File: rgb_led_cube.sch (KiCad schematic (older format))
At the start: 90 parts, among them Q1 IRLML6401TRPBF, Q10 MMBT2222A-TP, Q11 IRLML6401TRPBF, Q12 MMBT2222A-TP, Q13 IRLML6401TRPBF, Q14 MMBT2222A-TP, Q15 IRLML6401TRPBF, Q16 MMBT2222A-TP, Q2 MMBT2222A-TP, Q3 IRLML6401TRPBF, Q4 MMBT2222A-TP, Q5 IRLML6401TRPBF, Q6 MMBT2222A-TP, Q7 IRLML6401TRPBF, Q8 MMBT2222A-TP, Q9 IRLML6401TRPBF, U1 TLC59711PWPR, U10 TLC59711PWPR, U11 TLC59711PWPR, U12 TLC59711PWPR, U13 TLC59711PWPR, U14 TLC59711PWPR, U15 TLC59711PWPR, U16 TLC59711PWPR, U2 TLC59711PWPR, U3 TLC59711PWPR, U4 TLC59711PWPR, U5 TLC59711PWPR, U6 TLC59711PWPR, U7 TLC59711PWPR, U8 TLC59711PWPR, U9 TLC59711PWPR

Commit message: Update components placement
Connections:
- net at R20.2: now also CNTL1.13 (G12)
- net at R17.2: now also CNTL1.15 (G13)
- net at R23.2: now also CNTL1.12 (G14)
- net at R26.2: now also CNTL1.11 (G27)
- net at R29.2: now also CNTL1.10 (G26)
- net at R32.2: now also CNTL1.9 (G25)
- net at R35.2: now also CNTL1.8 (G33)
- net at R38.2: now also CNTL1.7 (G32)
- no-connect marks 2 -> 23
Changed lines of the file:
@@
 Wire Wire Line
 	11400 8450 10950 8450
+Wire Wire Line
+	9450 9750 8950 9750
+Wire Wire Line
+	8950 9750 8950 1350
+Wire Wire Line
+	8950 1350 9950 1350
+Wire Wire Line
+	9450 9550 9000 9550
+Wire Wire Line
+	9000 9550 9000 2150
+Wire Wire Line
+	9000 2150 9950 2150
+Wire Wire Line
+	9950 2950 9050 2950
+Wire Wire Line
+	9050 2950 9050 9450
+Wire Wire Line
+	9050 9450 9450 9450
+Wire Wire Line
+	9450 9350 9100 9350
+Wire Wire Line
+	9100 9350 9100 3750
+Wire Wire Line
+	9100 3750 9950 3750
+Wire Wire Line
+	9450 9250 9150 9250
+Wire Wire Line
+	9150 9250 9150 4550
+Wire Wire Line
+	9150 4550 9950 4550
+Wire Wire Line
+	9450 9150 9200 9150
+Wire Wire Line
+	9200 9150 9200 5350
+Wire Wire Line
+	9200 5350 9950 5350
+Wire Wire Line
+	9450 9050 9250 9050
+Wire Wire Line
+	9250 9050 9250 6150
+Wire Wire Line
+	9250 6150 9950 6150
+Wire Wire Line
+	9450 8950 9300 8950
+Wire Wire Line
+	9300 8950 9300 6950
+Wire Wire Line
+	9300 6950 9950 6950
+NoConn ~ 10950 10150
+NoConn ~ 10950 10050
+NoConn ~ 10950 9950
+NoConn ~ 10950 9850
+NoConn ~ 10950 9750
+NoConn ~ 10950 9650
+NoConn ~ 10950 9550
+NoConn ~ 10950 9450
+NoConn ~ 10950 9350
+NoConn ~ 10950 9250
+NoConn ~ 10950 9050
+NoConn ~ 10950 8850
+NoConn ~ 10950 8750
+NoConn ~ 10950 8650
+NoConn ~ 10950 8550
+NoConn ~ 9450 9850
+NoConn ~ 9450 9950
+NoConn ~ 9450 8350
+NoConn ~ 9450 8450
+NoConn ~ 9450 8550
+NoConn ~ 9450 8650
 $EndSCHEMATC

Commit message: Route ICs
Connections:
- net GND: no longer CNTL1.18 (CMD)
- no-connect marks 23 -> 24
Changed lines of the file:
@@
-$EndComp
-$Comp
-L power:GND #PWR0132
-U 1 1 5EAE4677
-P 9450 10050
-F 0 "#PWR0132" H 9450 9800 50  0001 C CNN
-F 1 "GND" V 9455 9922 50  0000 R CNN
-F 2 "" H 9450 10050 50  0001 C CNN
-F 3 "" H 9450 10050 50  0001 C CNN
-	1    9450 10050
-	0    1    1    0
 $EndComp
 $Comp
@@
 NoConn ~ 9450 8550
 NoConn ~ 9450 8650
+NoConn ~ 9450 10050
 $EndSCHEMATC

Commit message: Route pcb
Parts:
- Q1, Q10, Q11, Q12, Q13, Q14, Q15, Q16, Q2, Q3, Q4, Q5, Q6, Q7, Q8, Q9: footprint digikey-footprints:SOT-23-3 -> Package_TO_SOT_SMD:SOT-23
- U1, U10, U11, U12, U13, U14, U15, U16, U2, U3, U4, U5, U6, U7, U8, U9: footprint digikey-footprints:TSSOP-20-1EP_W4.4mm -> Package_SO:HTSSOP-20-1EP_4.4x6.5mm_P0.65mm_EP3.4x6.5mm_Mask2.75x3.43mm_ThermalVias

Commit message: Connect unused header pins to GND
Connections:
- net GND: now also CNTL1.39, CNTL1.40
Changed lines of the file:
@@
 NoConn ~ 9450 8650
 NoConn ~ 9450 10050
+$Comp
+L power:GND #PWR?
+U 1 1 5EAE9B47
+P 9950 10450
+F 0 "#PWR?" H 9950 10200 50  0001 C CNN
+F 1 "GND" H 9955 10277 50  0000 C CNN
+F 2 "" H 9950 10450 50  0001 C CNN
+F 3 "" H 9950 10450 50  0001 C CNN
+	1    9950 10450
+	1    0    0    -1
+$EndComp
+$Comp
+L power:GND #PWR?
+U 1 1 5EAEB6F4
+P 10050 10450
+F 0 "#PWR?" H 10050 10200 50  0001 C CNN
+F 1 "GND" H 10055 10277 50  0000 C CNN
+F 2 "" H 10050 10450 50  0001 C CNN
+F 3 "" H 10050 10450 50  0001 C CNN
+	1    10050 10450
+	1    0    0    -1
+$EndComp
 $EndSCHEMATC

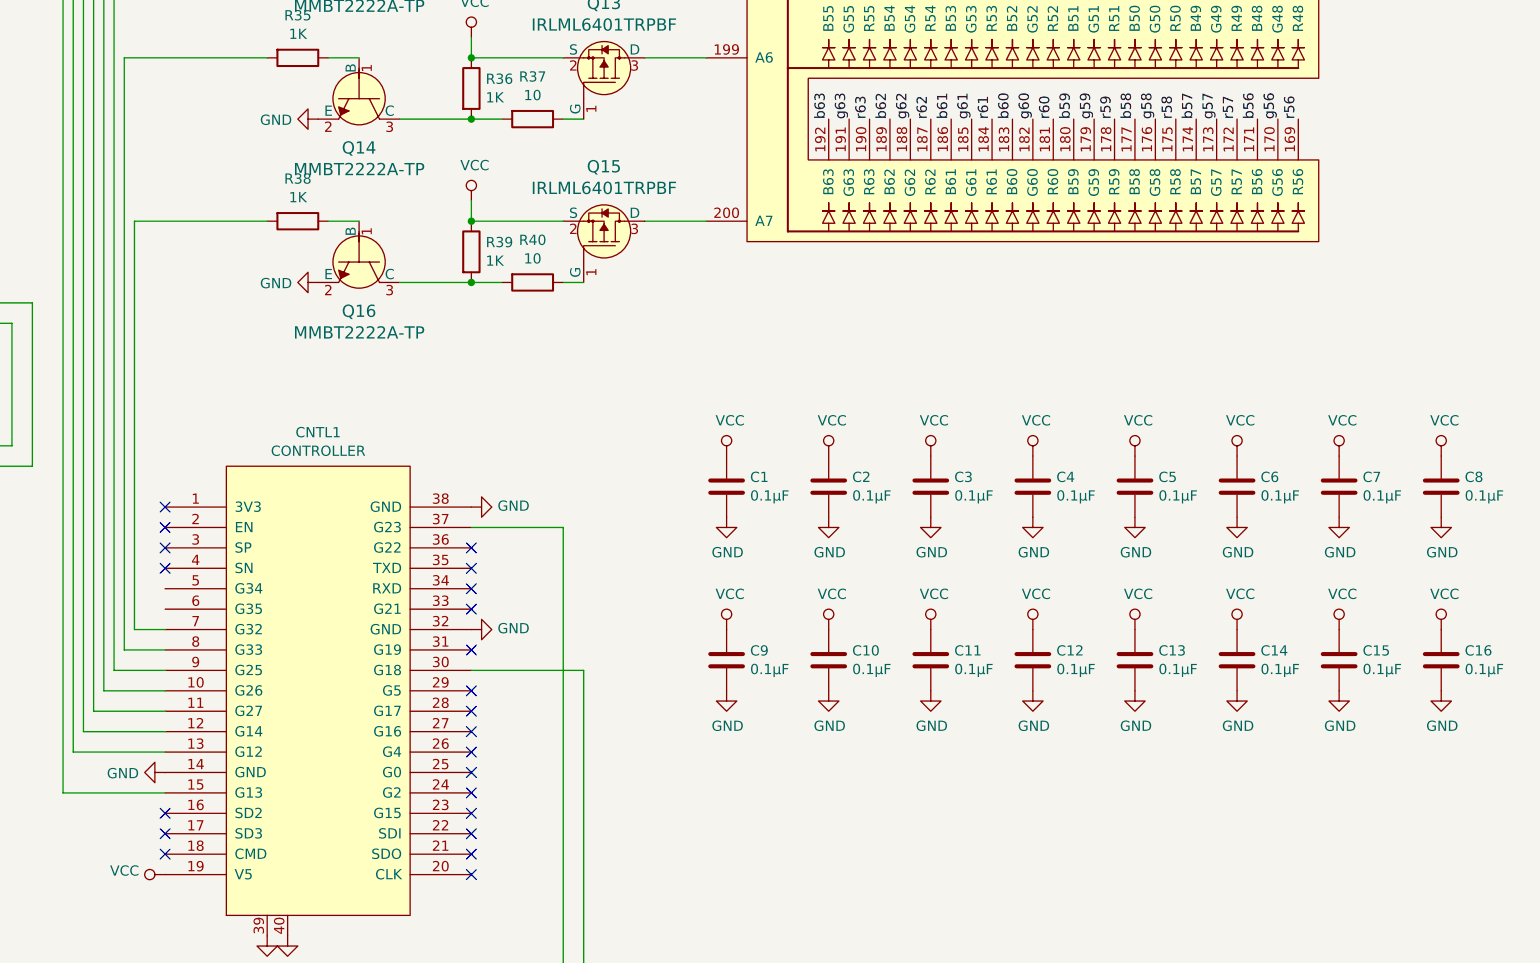
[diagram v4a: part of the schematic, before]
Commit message: Add microphone
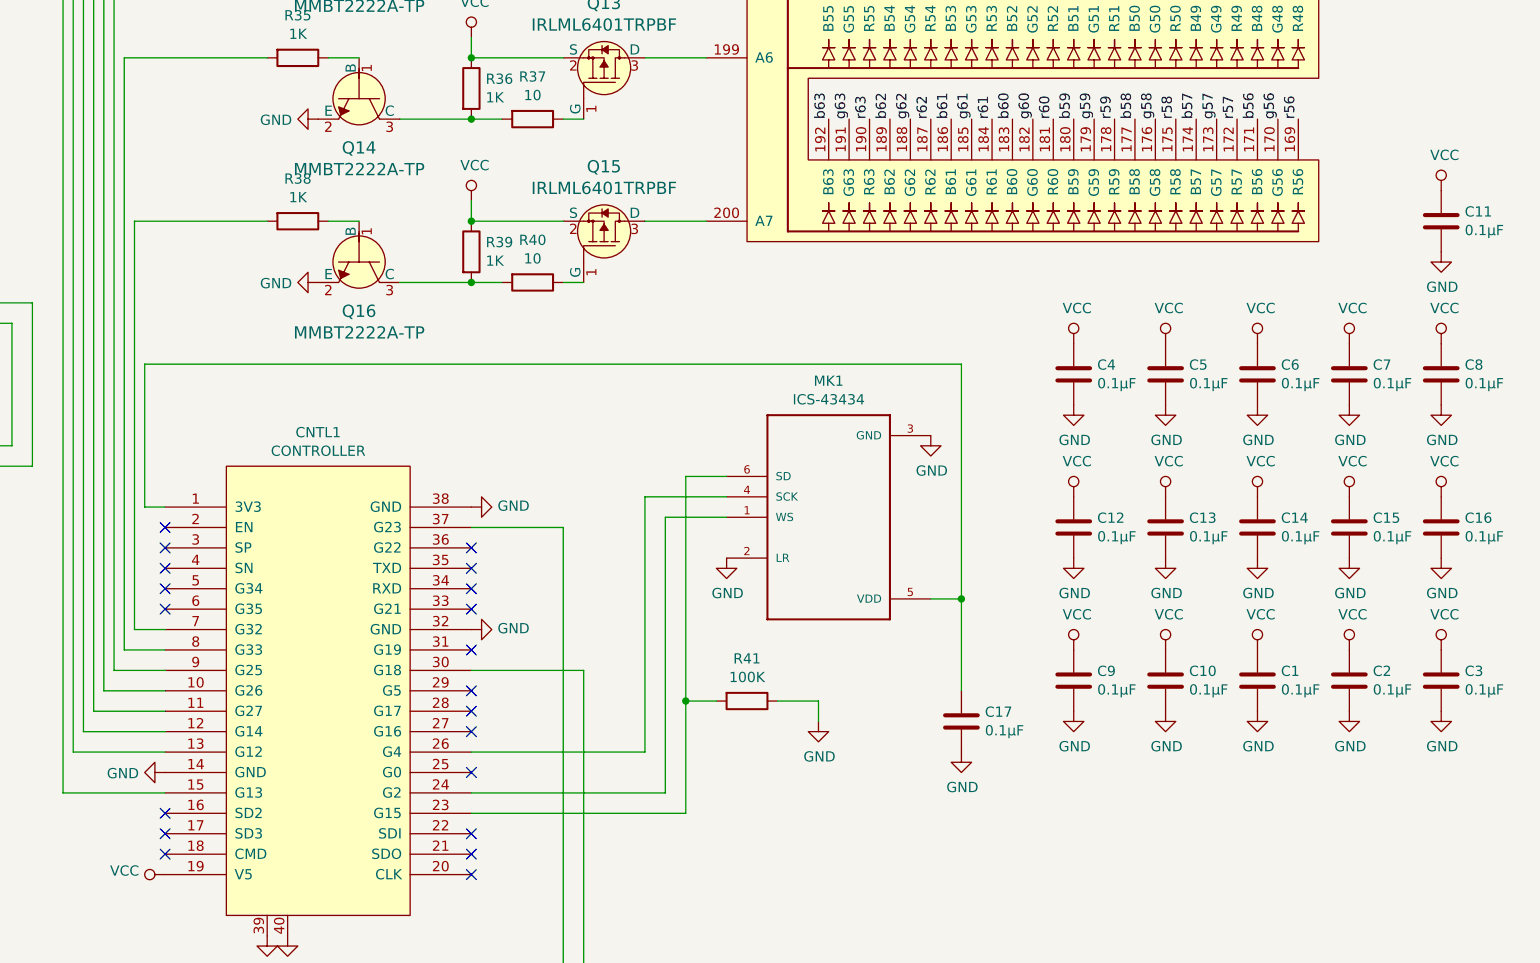
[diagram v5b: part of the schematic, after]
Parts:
- added C17: 0.1µF, Capacitor_SMD:C_0805_2012Metric_Pad1.15x1.40mm_HandSolder, symbol Device:C
- added MK1: ICS-43434, rgb_led_cube:MIC_ICS-43434, symbol rgb_led_cube:ICS-43434
- added R41: 100K, Resistor_SMD:R_0805_2012Metric_Pad1.15x1.40mm_HandSolder, symbol Device:R
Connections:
- net GND: now also C17.2, MK1.2 (LR), MK1.3 (GND), R41.1
- net at CNTL1.1 (3V3): now also C17.1, MK1.5 (VDD)
- net at CNTL1.23 (G15): now also MK1.6 (SD), R41.2
- net at CNTL1.24 (G2): now also MK1.1 (WS)
- net at CNTL1.26 (G4): now also MK1.4 (SCK)
- no-connect marks 24 -> 22
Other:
- moved on the sheet: C1, C10, C11, C12, C13, C14, C15, C16, C2, C3, C4, C5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

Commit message: Update layout
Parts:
- added J1: OSTTC022162, digikey-footprints:Term_Block_1x2_P5.08MM, symbol dk_Terminal-Blocks-Wire-to-Board:OSTTC022162
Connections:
- net GND: now also J1.1
- net VCC: now also J1.2
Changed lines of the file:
@@
 Wire Wire Line
 	12650 9300 12450 9300
+$Comp
+L dk_Terminal-Blocks-Wire-to-Board:OSTTC022162 J1
+U 1 1 5EBAD8B8
+P 15550 6000
+F 0 "J1" V 15325 5983 50  0000 C CNN
+F 1 "OSTTC022162" V 15416 5983 50  0000 C CNN
+F 2 "digikey-footprints:Term_Block_1x2_P5.08MM" H 15750 6200 60  0001 L CNN
+F 3 "http://www.on-shore.com/wp-content/uploads/OSTTCXX2162.pdf" H 15750 6300 60  0001 L CNN
+F 4 "ED2609-ND" H 15750 6400 60  0001 L CNN "Digi-Key_PN"
+F 5 "OSTTC022162" H 15750 6500 60  0001 L CNN "MPN"
+F 6 "Connectors, Interconnects" H 15750 6600 60  0001 L CNN "Category"
+F 7 "Terminal Blocks - Wire to Board" H 15750 6700 60  0001 L CNN "Family"
+F 8 "http://www.on-shore.com/wp-content/uploads/OSTTCXX2162.pdf" H 15750 6800 60  0001 L CNN "DK_Datasheet_Link"
+F 9 "/product-detail/en/on-shore-technology-inc/OSTTC022162/ED2609-ND/614558" H 15750 6900 60  0001 L CNN "DK_Detail_Page"
+F 10 "TERM BLK 2P SIDE ENT 5.08MM PCB" H 15750 7000 60  0001 L CNN "Description"
+F 11 "On Shore Technology Inc." H 15750 7100 60  0001 L CNN "Manufacturer"
+F 12 "Active" H 15750 7200 60  0001 L CNN "Status"
+	1    15550 6000
+	0    1    1    0
+$EndComp
+$Comp
+L power:VCC #PWR0139
+U 1 1 5EBB23F5
+P 15650 6100
+F 0 "#PWR0139" H 15650 5950 50  0001 C CNN
+F 1 "VCC" V 15667 6228 50  0000 L CNN
+F 2 "" H 15650 6100 50  0001 C CNN
+F 3 "" H 15650 6100 50  0001 C CNN
+	1    15650 6100
+	0    1    1    0
+$EndComp
+$Comp
+L power:GND #PWR0140
+U 1 1 5EBB41A8
+P 15650 6000
+F 0 "#PWR0140" H 15650 5750 50  0001 C CNN
+F 1 "GND" V 15655 5872 50  0000 R CNN
+F 2 "" H 15650 6000 50  0001 C CNN
+F 3 "" H 15650 6000 50  0001 C CNN
+	1    15650 6000
+	0    -1   -1   0
+$EndComp
 $EndSCHEMATC

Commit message: Add Mounting holes
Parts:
- added H1, H2, H3, H4: MountingHole_Pad, MountingHole:MountingHole_3.2mm_M3_Pad_Via, symbol Mechanical:MountingHole_Pad
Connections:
- net GND: now also H1.1, H2.1, H3.1, H4.1
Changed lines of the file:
@@
 	0    -1   -1   0
 $EndComp
+$Comp
+L Mechanical:MountingHole_Pad H1
+U 1 1 5ED7C02E
+P 15400 4450
+F 0 "H1" H 15500 4499 50  0000 L CNN
+F 1 "MountingHole_Pad" H 15500 4408 50  0000 L CNN
+F 2 "MountingHole:MountingHole_3.2mm_M3_Pad_Via" H 15400 4450 50  0001 C CNN
+F 3 "~" H 15400 4450 50  0001 C CNN
+	1    15400 4450
+	1    0    0    -1
+$EndComp
+$Comp
+L Mechanical:MountingHole_Pad H2
+U 1 1 5ED803AA
+P 15750 4450
+F 0 "H2" H 15750 4737 50  0000 C CNN
+F 1 "MountingHole_Pad" H 15750 4646 50  0000 C CNN
+F 2 "MountingHole:MountingHole_3.2mm_M3_Pad_Via" H 15750 4450 50  0001 C CNN
+F 3 "~" H 15750 4450 50  0001 C CNN
+	1    15750 4450
+	1    0    0    -1
+$EndComp
+$Comp
+L Mechanical:MountingHole_Pad H3
+U 1 1 5ED809D9
+P 15400 5350
+F 0 "H3" H 15500 5399 50  0000 L CNN
+F 1 "MountingHole_Pad" H 15500 5308 50  0000 L CNN
+F 2 "MountingHole:MountingHole_3.2mm_M3_Pad_Via" H 15400 5350 50  0001 C CNN
+F 3 "~" H 15400 5350 50  0001 C CNN
+	1    15400 5350
+	1    0    0    -1
+$EndComp
+$Comp
+L Mechanical:MountingHole_Pad H4
+U 1 1 5ED812DA
+P 15750 5350
+F 0 "H4" H 15750 5637 50  0000 C CNN
+F 1 "MountingHole_Pad" H 15750 5546 50  0000 C CNN
+F 2 "MountingHole:MountingHole_3.2mm_M3_Pad_Via" H 15750 5350 50  0001 C CNN
+F 3 "~" H 15750 5350 50  0001 C CNN
+	1    15750 5350
+	1    0    0    -1
+$EndComp
+$Comp
+L power:GND #PWR0141
+U 1 1 5ED82CB4
+P 15400 4550
+F 0 "#PWR0141" H 15400 4300 50  0001 C CNN
+F 1 "GND" H 15405 4377 50  0000 C CNN
+F 2 "" H 15400 4550 50  0001 C CNN
+F 3 "" H 15400 4550 50  0001 C CNN
+	1    15400 4550
+	1    0    0    -1
+$EndComp
+$Comp
+L power:GND #PWR0142
+U 1 1 5ED841EE
+P 15750 4550
+F 0 "#PWR0142" H 15750 4300 50  0001 C CNN
+F 1 "GND" H 15755 4377 50  0000 C CNN
+F 2 "" H 15750 4550 50  0001 C CNN
+F 3 "" H 15750 4550 50  0001 C CNN
+	1    15750 4550
+	1    0    0    -1
+$EndComp
+$Comp
+L power:GND #PWR0143
+U 1 1 5ED85723
+P 15400 5450
+F 0 "#PWR0143" H 15400 5200 50  0001 C CNN
+F 1 "GND" H 15405 5277 50  0000 C CNN
+F 2 "" H 15400 5450 50  0001 C CNN
+F 3 "" H 15400 5450 50  0001 C CNN
+	1    15400 5450
+	1    0    0    -1
+$EndComp
+$Comp
+L power:GND #PWR0144
+U 1 1 5ED86C64
+P 15750 5450
+F 0 "#PWR0144" H 15750 5200 50  0001 C CNN
+F 1 "GND" H 15755 5277 50  0000 C CNN
+F 2 "" H 15750 5450 50  0001 C CNN
+F 3 "" H 15750 5450 50  0001 C CNN
+	1    15750 5450
+	1    0    0    -1
+$EndComp
 $EndSCHEMATC
